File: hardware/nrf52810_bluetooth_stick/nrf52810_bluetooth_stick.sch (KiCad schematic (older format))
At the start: 16 parts

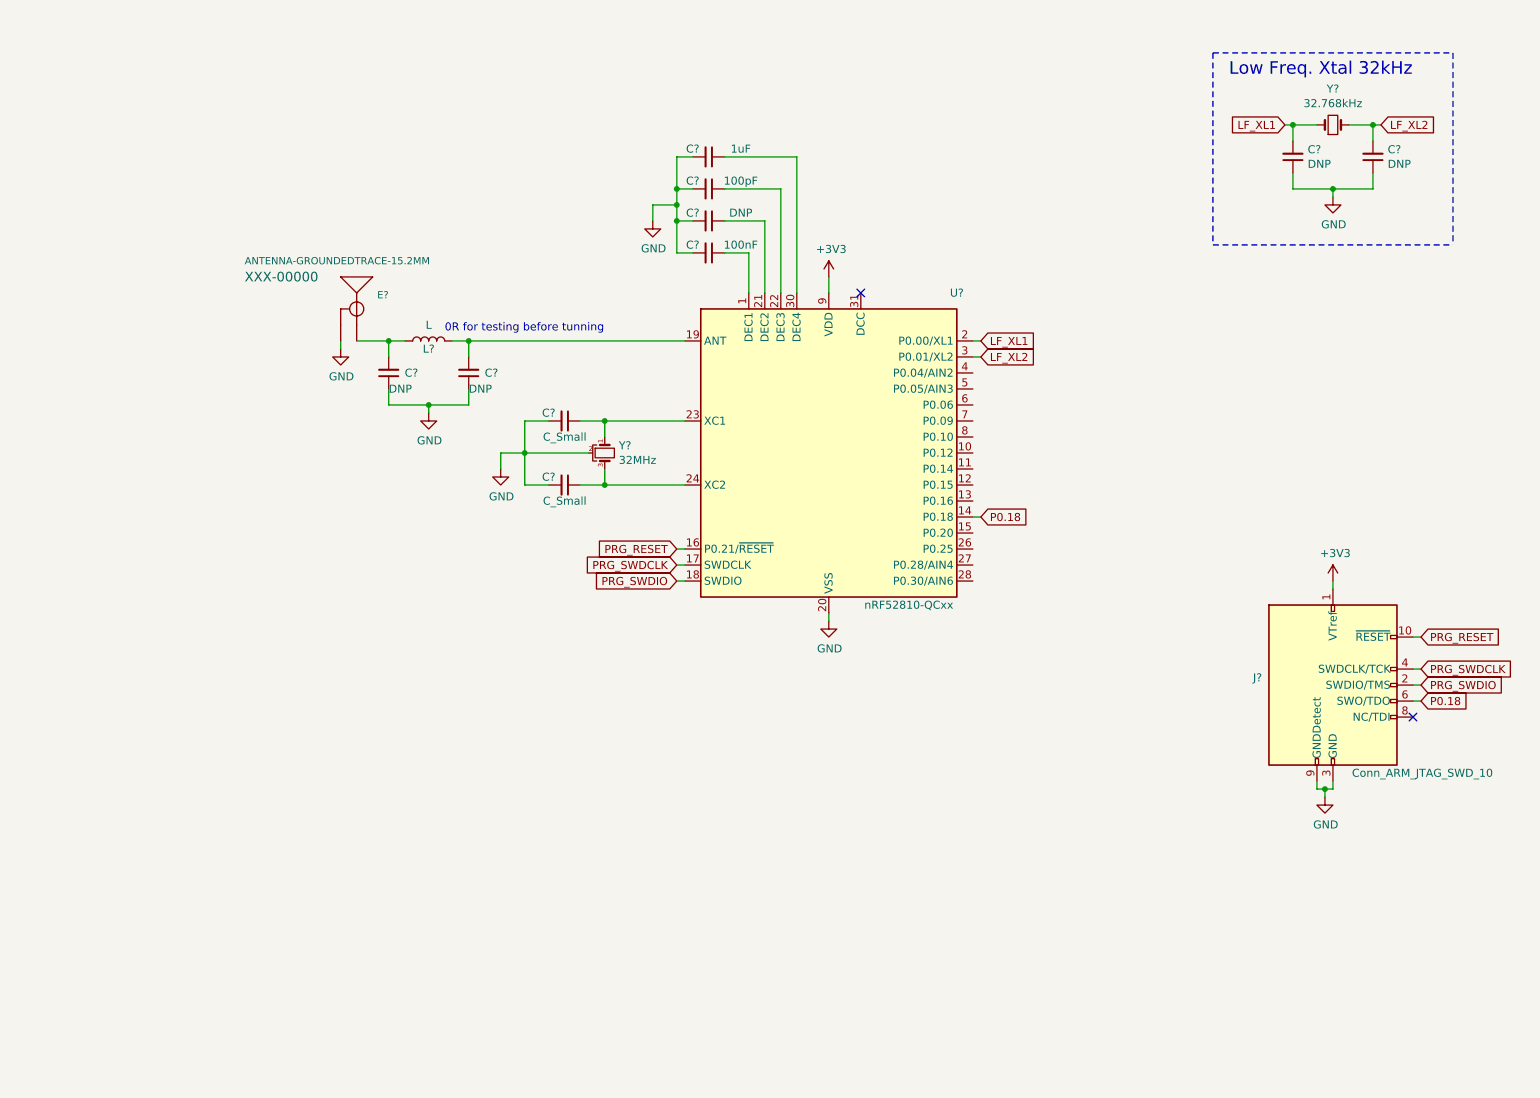
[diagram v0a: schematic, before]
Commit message: Added li-ion charging circuit
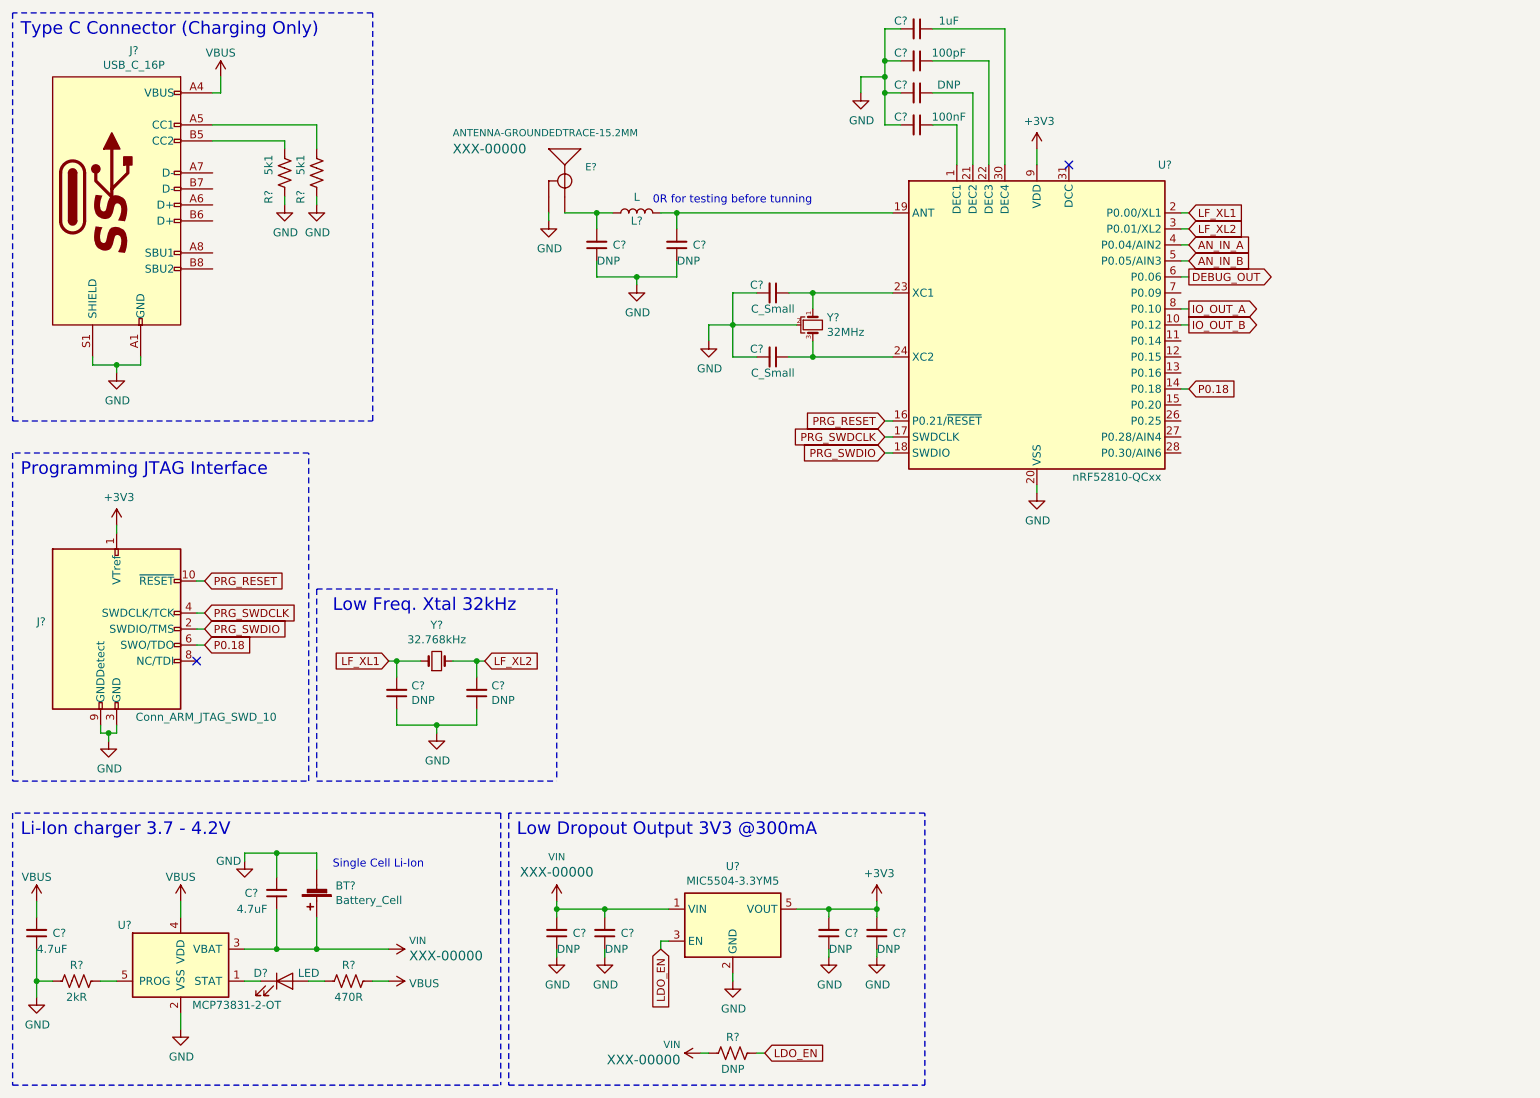
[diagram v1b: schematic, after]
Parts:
- added BT?: Battery_Cell, symbol Device:Battery_Cell
- added C? (x4): DNP, symbol Device:C_Small
- added C? (x2): 4.7uF, symbol Device:C_Small
- added D?: LED, symbol Device:LED
- added J?: USB_C_16P, symbol Connector:USB_C_16P
- added R?: DNP, symbol Device:R_US
- added R?: 2kR, symbol Device:R_US
- added R?: 470R, symbol Device:R_US
- added R? (x2): 5k1, symbol Device:R_US
- added U?: MIC5504-3.3YM5, Package_TO_SOT_SMD:SOT-23-5, symbol Regulator_Linear:MIC5504-3.3YM5
- added U?: MCP73831-2-OT, Package_TO_SOT_SMD:SOT-23-5, symbol Battery_Management:MCP73831-2-OT
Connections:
- net +3V3: now also C?.2, C?.2, U?.5 (VOUT)
- net GND: now also BT?.2 (-), C?.1, C?.1, C?.1, C?.1, C?.1, C?.2, J?.A1 (GND), J?.A12 (GND), J?.B1 (GND), J?.B12 (GND), J?.S1 (SHIELD), R?.1, R?.1, R?.1, U?.2 (GND), U?.2 (VSS)
- net IO_OUT_B: now reaches U?.10 (P0.12)
- net AN_IN_A: now reaches U?.4 (P0.04/AIN2)
- net AN_IN_B: now reaches U?.5 (P0.05/AIN3)
- net DEBUG_OUT: now reaches U?.6 (P0.06)
- net IO_OUT_A: now reaches U?.8 (P0.10)
- new net: D?.1 (K), U?.1 (STAT)
- new net: R?.2, U?.5 (PROG)
- new net: D?.2 (A), R?.1
- new net: J?.A5 (CC1), R?.2
- new net: J?.B5 (CC2), R?.2
- new net LDO_EN: R?.1, U?.3 (EN)
- new net VBUS: C?.2, J?.A4 (VBUS), J?.A9 (VBUS), J?.B4 (VBUS), J?.B9 (VBUS), R?.2, U?.4 (VDD)
- new net VIN: BT?.1 (+), C?.1, C?.2, C?.2, R?.2, U?.1 (VIN), U?.3 (VBAT)
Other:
- note added: "Li-Ion charger 3.7 - 4.2V"
- note added: "Low Dropout Output 3V3 @300mA"
- note added: "Programming JTAG Interface"
- note added: "Single Cell Li-Ion"
- note added: "Type C Connector (Charging Only)"
- moved on the sheet: C?, E?, J?, L?, U?, Y?

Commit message: Template update...
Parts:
- added D?: LED, symbol Device:LED
- added R?: 470R, symbol Device:R_US
- J?: footprint (none) -> Connector_PinHeader_1.27mm:PinHeader_2x05_P1.27mm_Vertical_SMD
- J?: footprint (none) -> Connector_USB:USB_C_Receptacle_Palconn_UTC16-G
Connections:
- net +3V3: now also R?.2
- net GND: now also D?.1 (K)
- new net: D?.2 (A), R?.1
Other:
- note added: "https://www.sparkfun.com/datasheets/BreakoutBoards/ADMP401-Breakout-v13.pdf"
- moved on the sheet: C?, Y?
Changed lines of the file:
@@
 L Device:Crystal_GND2_Small Y?
 U 1 1 5EA575AD
-P 5850 2900
-F 0 "Y?" V 5804 2988 50  0000 L CNN
-F 1 "32MHz" V 5895 2988 50  0000 L CNN
-F 2 "" H 5850 2900 50  0001 C CNN
-F 3 "~" H 5850 2900 50  0001 C CNN
-	1    5850 2900
+P 6050 2900
+F 0 "Y?" V 6004 2988 50  0000 L CNN
+F 1 "32MHz" V 6095 2988 50  0000 L CNN
+F 2 "" H 6050 2900 50  0001 C CNN
+F 3 "~" H 6050 2900 50  0001 C CNN
+	1    6050 2900
 	0    1    1    0
 $EndComp
 Wire Wire Line
-	5850 2800 5850 2700
-Wire Wire Line
-	5850 2700 6350 2700
-Wire Wire Line
-	5850 3000 5850 3100
-Wire Wire Line
-	5850 3100 6350 3100
+	6050 2800 6050 2700
+Wire Wire Line
+	6050 3000 6050 3100
 $Comp
 L Device:C_Small C?
 U 1 1 5EA5940D
-P 5600 2700
-F 0 "C?" V 5550 2600 50  0000 C CNN
-F 1 "C_Small" V 5700 2700 50  0000 C CNN
-F 2 "" H 5600 2700 50  0001 C CNN
-F 3 "~" H 5600 2700 50  0001 C CNN
-	1    5600 2700
+P 5800 2700
+F 0 "C?" V 5750 2600 50  0000 C CNN
+F 1 "C_Small" V 5900 2700 50  0000 C CNN
+F 2 "" H 5800 2700 50  0001 C CNN
+F 3 "~" H 5800 2700 50  0001 C CNN
+	1    5800 2700
 	0    1    1    0
 $EndComp
@@
 L Device:C_Small C?
 U 1 1 5EA5A037
-P 5600 3100
-F 0 "C?" V 5550 3000 50  0000 C CNN
-F 1 "C_Small" V 5700 3100 50  0000 C CNN
-F 2 "" H 5600 3100 50  0001 C CNN
-F 3 "~" H 5600 3100 50  0001 C CNN
-	1    5600 3100
+P 5800 3100
+F 0 "C?" V 5750 3000 50  0000 C CNN
+F 1 "C_Small" V 5900 3100 50  0000 C CNN
+F 2 "" H 5800 3100 50  0001 C CNN
+F 3 "~" H 5800 3100 50  0001 C CNN
+	1    5800 3100
 	0    1    1    0
 $EndComp
 Wire Wire Line
-	5700 2700 5850 2700
-Connection ~ 5850 2700
-Wire Wire Line
-	5700 3100 5850 3100
-Connection ~ 5850 3100
-Wire Wire Line
-	5500 2700 5350 2700
-Wire Wire Line
-	5350 2700 5350 2900
-Wire Wire Line
-	5350 3100 5500 3100
-Wire Wire Line
-	5750 2900 5350 2900
-Connection ~ 5350 2900
-Wire Wire Line
-	5350 2900 5350 3100
+	5900 2700 6050 2700
+Wire Wire Line
+	5900 3100 6050 3100
+Wire Wire Line
+	5700 2700 5550 2700
+Wire Wire Line
+	5550 2700 5550 2900
+Wire Wire Line
+	5550 3100 5700 3100
+Wire Wire Line
+	5950 2900 5550 2900
+Connection ~ 5550 2900
+Wire Wire Line
+	5550 2900 5550 3100
 $Comp
 L power:GND #PWR?
 U 1 1 5EA5AA9B
-P 5200 3000
-F 0 "#PWR?" H 5200 2750 50  0001 C CNN
-F 1 "GND" H 5205 2827 50  0000 C CNN
-F 2 "" H 5200 3000 50  0001 C CNN
-F 3 "" H 5200 3000 50  0001 C CNN
-	1    5200 3000
-	1    0    0    -1
-$EndComp
-Wire Wire Line
-	5350 2900 5200 2900
-Wire Wire Line
-	5200 2900 5200 3000
+P 5400 3000
+F 0 "#PWR?" H 5400 2750 50  0001 C CNN
+F 1 "GND" H 5405 2827 50  0000 C CNN
+F 2 "" H 5400 3000 50  0001 C CNN
+F 3 "" H 5400 3000 50  0001 C CNN
+	1    5400 3000
+	1    0    0    -1
+$EndComp
+Wire Wire Line
+	5550 2900 5400 2900
+Wire Wire Line
+	5400 2900 5400 3000
 Wire Wire Line
 	6350 3500 6300 3500
@@
 F 0 "J?" H 1057 4846 50  0000 R CNN
 F 1 "Conn_ARM_JTAG_SWD_10" H 2500 4250 50  0000 R CNN
-F 2 "" H 1500 4800 50  0001 C CNN
+F 2 "Connector_PinHeader_1.27mm:PinHeader_2x05_P1.27mm_Vertical_SMD" H 1500 4800 50  0001 C CNN
 F 3 "http://infocenter.arm.com/help/topic/com.arm.doc.ddi0314h/DDI0314H_coresight_components_trm.pdf" V 1150 3550 50  0001 C CNN
 	1    1500 4800
@@
 	3950 5950 3950 7650
 Wire Notes Line
-	3950 7650 6550 7650
-Wire Notes Line
-	6550 7650 6550 5950
-Wire Notes Line
-	6550 5950 3950 5950
-Wire Notes Line
 	850  7650 3900 7650
 Wire Notes Line
@@
 F 0 "J?" H 1608 3715 50  0000 C CNN
 F 1 "USB_C_16P" H 1608 3624 50  0000 C CNN
-F 2 "" H 1650 2450 50  0001 C CNN
+F 2 "Connector_USB:USB_C_Receptacle_Palconn_UTC16-G" H 1650 2450 50  0001 C CNN
 F 3 "https://www.usb.org/sites/default/files/documents/usb_type-c.zip" H 1650 2450 50  0001 C CNN
 	1    1500 2450
@@
 Text GLabel 8200 2900 2    50   Output ~ 0
 IO_OUT_B
+$Comp
+L Device:LED D?
+U 1 1 5EC237B6
+P 6650 7150
+F 0 "D?" H 6500 7200 50  0000 C CNN
+F 1 "LED" H 6800 7200 50  0000 C CNN
+F 2 "" H 6650 7150 50  0001 C CNN
+F 3 "~" H 6650 7150 50  0001 C CNN
+	1    6650 7150
+	0    -1   -1   0
+$EndComp
+$Comp
+L Device:R_US R?
+U 1 1 5EC237BC
+P 6650 6750
+F 0 "R?" V 6750 6750 50  0000 C CNN
+F 1 "470R" V 6550 6750 50  0000 C CNN
+F 2 "" V 6690 6740 50  0001 C CNN
+F 3 "~" H 6650 6750 50  0001 C CNN
+	1    6650 6750
+	-1   0    0    1
+$EndComp
+Wire Wire Line
+	6650 7000 6650 6900
+Wire Wire Line
+	6250 6550 6650 6550
+Wire Wire Line
+	6650 6550 6650 6600
+$Comp
+L power:GND #PWR?
+U 1 1 5EC353F6
+P 6650 7350
+F 0 "#PWR?" H 6650 7100 50  0001 C CNN
+F 1 "GND" H 6655 7177 50  0000 C CNN
+F 2 "" H 6650 7350 50  0001 C CNN
+F 3 "" H 6650 7350 50  0001 C CNN
+	1    6650 7350
+	1    0    0    -1
+$EndComp
+Wire Wire Line
+	6650 7350 6650 7300
+Wire Notes Line
+	6850 7650 6850 5950
+Wire Notes Line
+	3950 7650 6850 7650
+Wire Notes Line
+	3950 5950 6850 5950
+Wire Wire Line
+	6350 2700 6050 2700
+Connection ~ 6050 2700
+Wire Wire Line
+	6350 3100 6050 3100
+Connection ~ 6050 3100
+Text Notes 5450 4900 0    50   ~ 0
+https://www.sparkfun.com/datasheets/BreakoutBoards/ADMP401-Breakout-v13.pdf
 $EndSCHEMATC
